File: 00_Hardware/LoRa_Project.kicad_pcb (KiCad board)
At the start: 4 copper layers, 60 x 45 mm, 87 parts, among them IC1 MAX17048G+T10, IC2 E22-900M22S, J1 Conn_01x04_Pin, J2 USB_C_Receptacle_USB2.0_16P, J3 Conn_01x04_Pin, J4 Header_01x02_2.0mm JST PH, J5 SMA_ST_SMD, J6 Conn_01x04_Pin, U1 TPS2116DRLR, U2 MIC5219-3.3YM5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

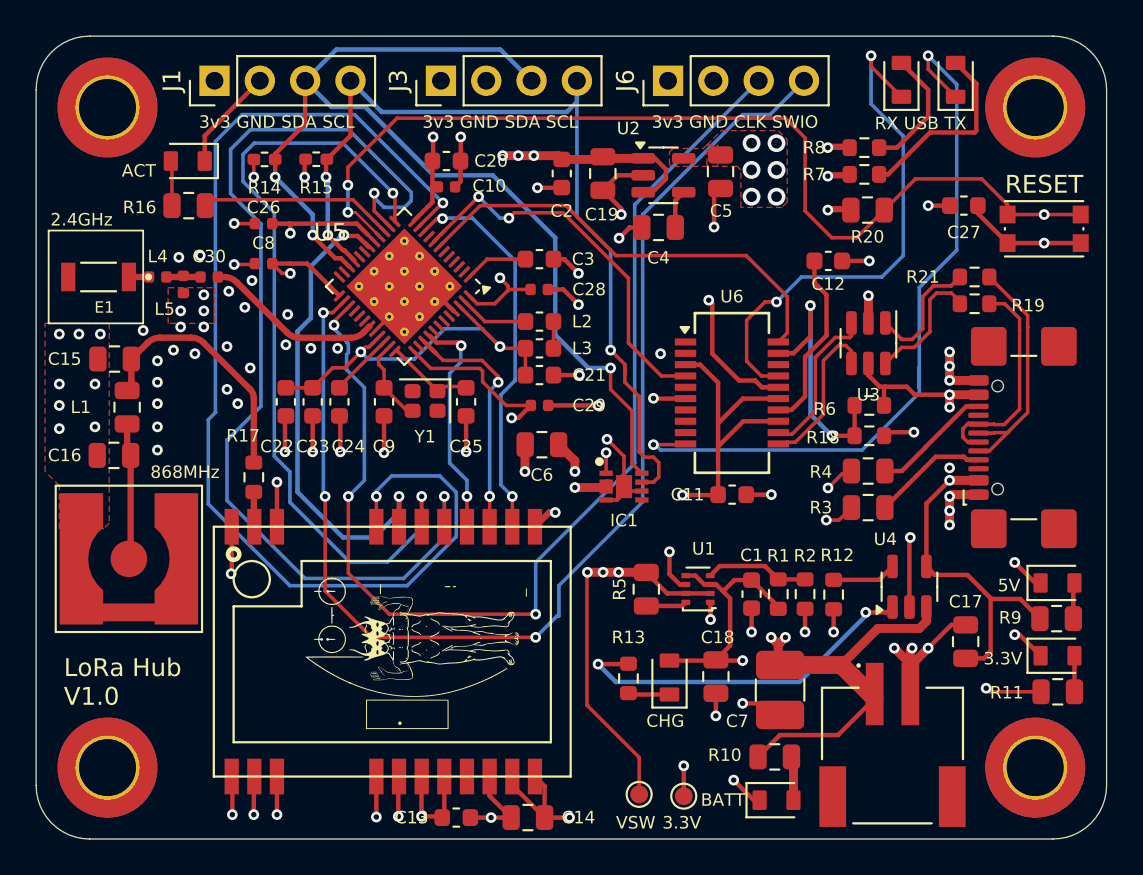
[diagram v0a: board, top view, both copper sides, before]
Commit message: Removed SMA for GPIO header placement.
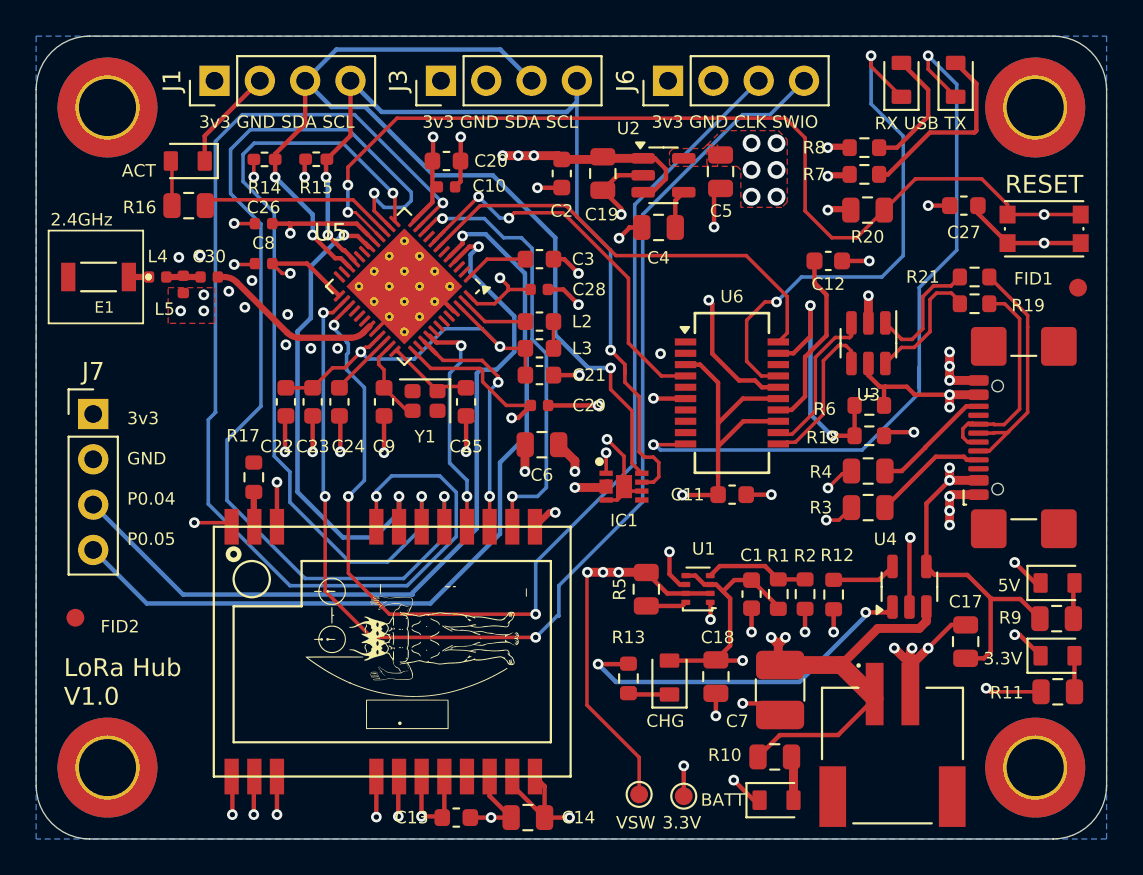
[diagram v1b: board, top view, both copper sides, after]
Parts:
- removed C15, C16: C_NP_0805, Project_Footprints:C_0805_2012Metric
- removed J5: SMA_ST_SMD, Project_Footprints:SMA_ST_SMD
- removed L1: L_jumper_0R, Project_Footprints:L_0805_2012Metric
- added FID1: Fiducial_1mm_Mask2mm, Fiducial:Fiducial_1mm_Mask2mm, F.Cu at (248.4, 66.1)
- added FID2: Fiducial_1mm_Mask2mm, Fiducial:Fiducial_1mm_Mask2mm, F.Cu at (192.2, 84.6)
- added J7: Conn_01x04_Pin, Connector_PinHeader_2.54mm:PinHeader_1x04_P2.54mm_Vertical, F.Cu at (193.2, 73.2)
- D2: value LED Green -> LED Blue
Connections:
- net Net-(R19-Pad2) renamed /Power/D_P
- net Net-(R21-Pad2) renamed /Power/D_N
- U5 pad 4: unconnected-(U5-P0.04-Pad4) -> P0.04
- U5 pad 5: unconnected-(U5-P0.05-Pad5) -> P0.05
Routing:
- net P0.05: track 0.00 -> 46.9 mm, vias 0 -> 1
- net P0.04: track 0.00 -> 45.3 mm, vias 0 -> 1
- net Net-(C15-Pad1): track 14.2 -> 0.00 mm
- net GND: track 154.7 -> 142.5 mm, vias 92 -> 70
- net Net-(J5-In): track 7.69 -> 0.00 mm
- net /nRF52840 and LoRa/LORA_IRQ: track 21.9 -> 24.6 mm
- added copper zone on B.Cu, net GND
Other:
- board text added: "3v3 GND P0.04 P0.05"
- board text removed: "868MHz"

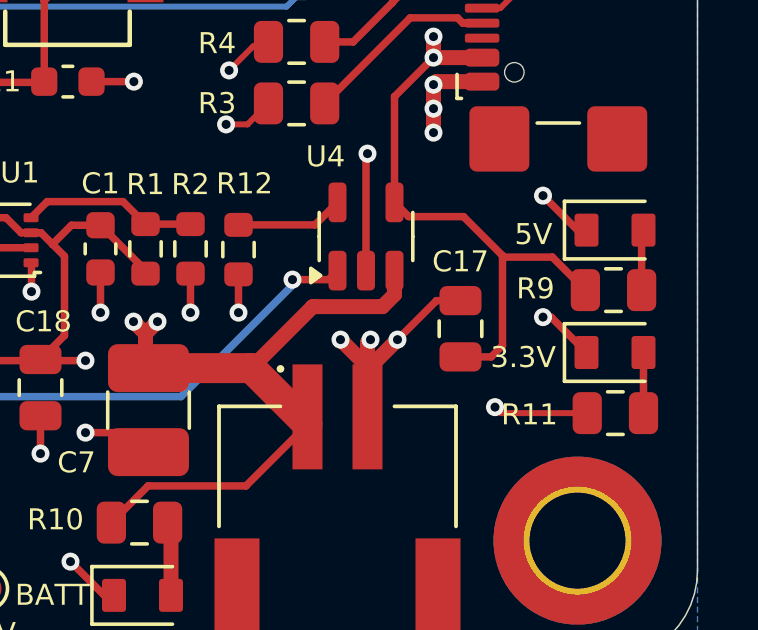
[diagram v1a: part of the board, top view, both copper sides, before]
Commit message: updated some library files/3d
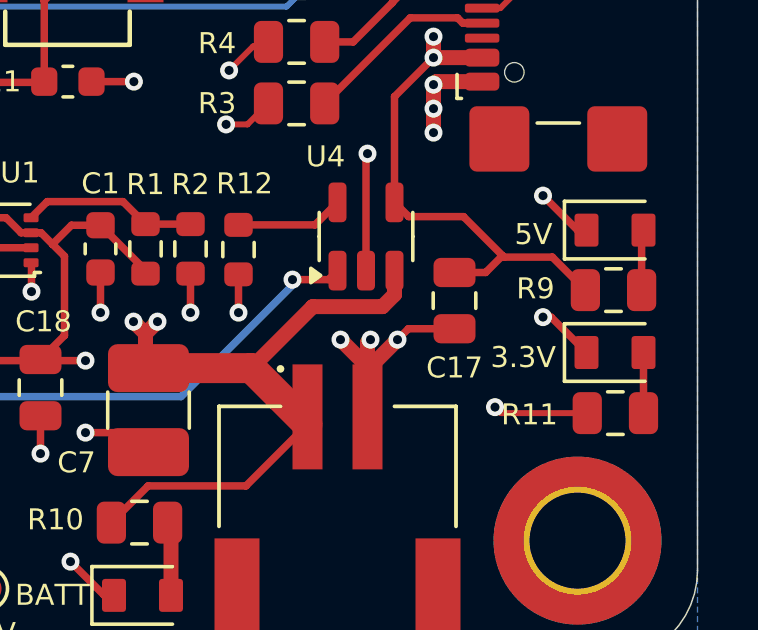
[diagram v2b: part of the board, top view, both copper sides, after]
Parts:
- moved C17 0.96 mm to (241.9, 85.0), turned to -90 degrees
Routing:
- net VBUS: track 69.0 -> 66.2 mm
- net GND: track 142.5 -> 141.9 mm

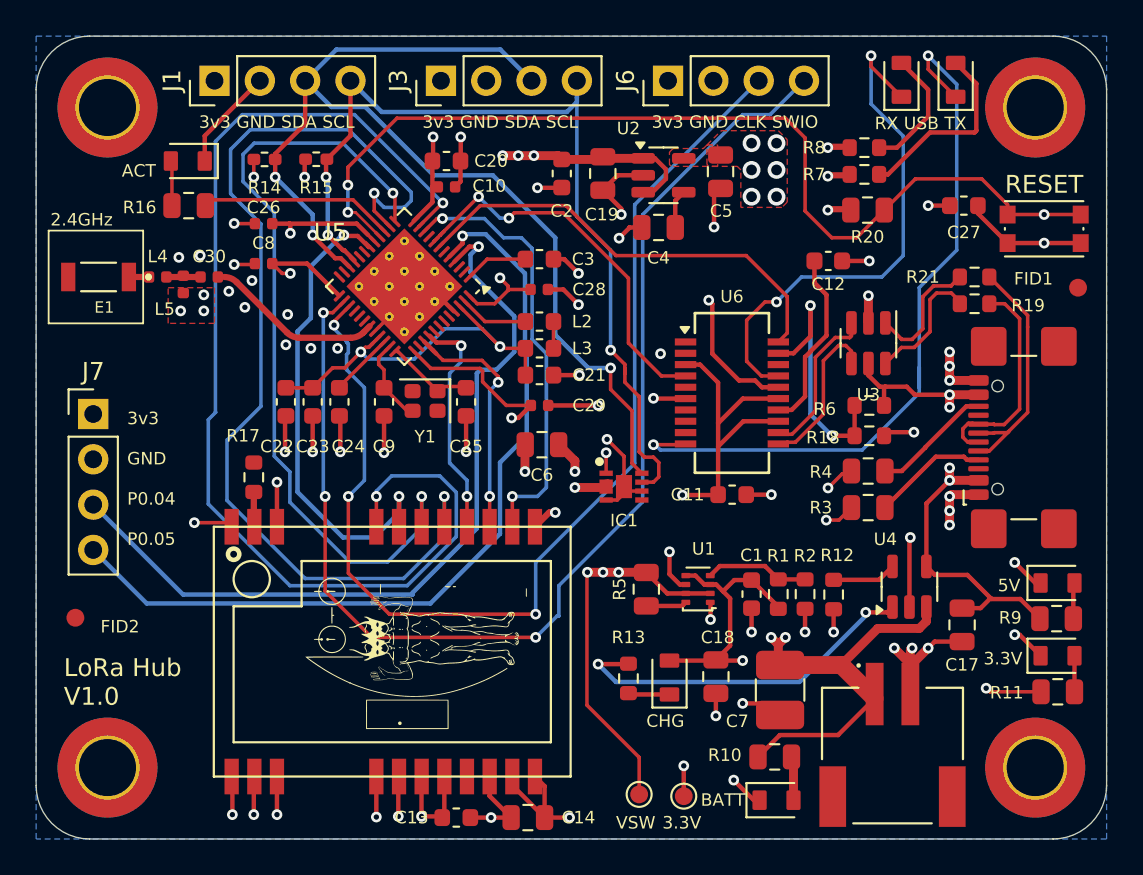
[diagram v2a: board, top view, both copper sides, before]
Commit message: Antenna output changed to fully isolate path
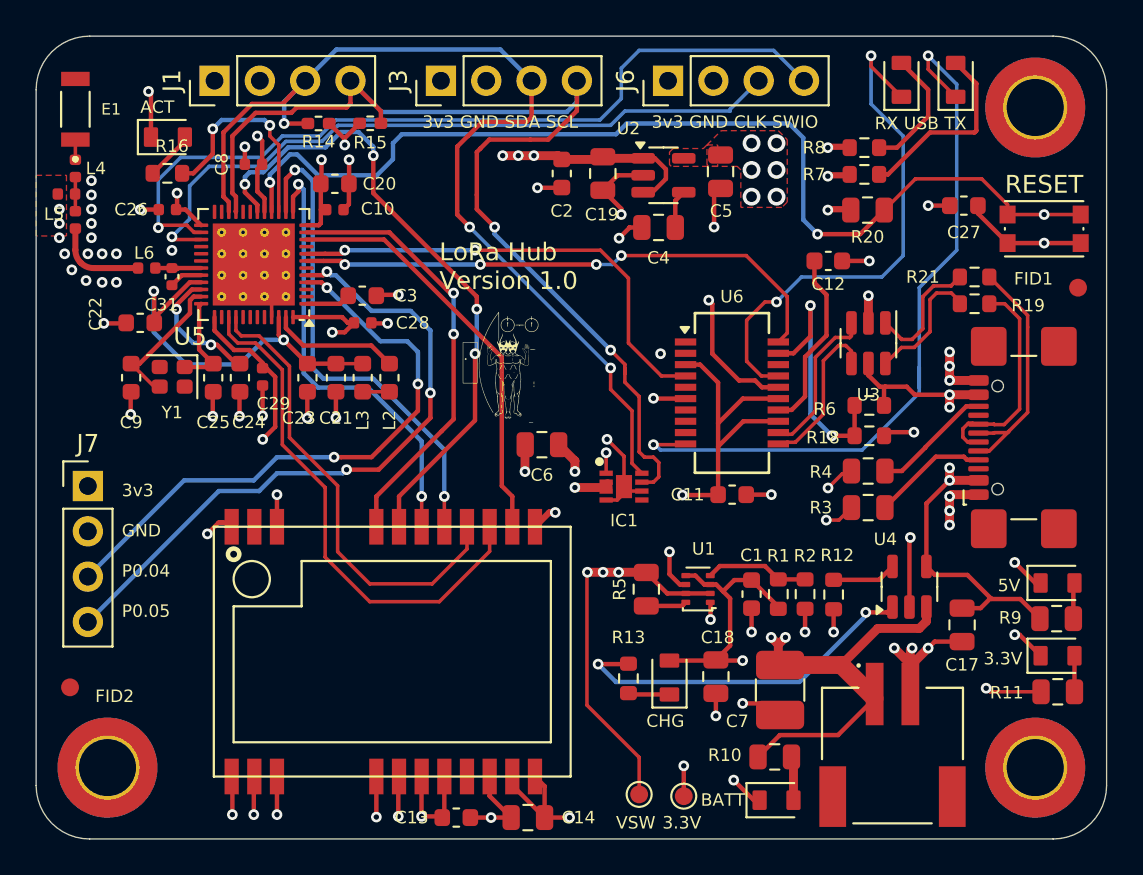
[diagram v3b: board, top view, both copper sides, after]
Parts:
- removed the G*** at (211.8, 86.1)
- removed H1: MountingHole_Pad_M3, MountingHole:MountingHole_3.2mm_M3_DIN965_Pad_TopBottom
- removed R17: 0R_0603, Resistor_SMD:R_0603_1608Metric
- added C31: 1pF, Capacitor_SMD:C_0402_1005Metric, F.Cu at (197.6, 65.5)
- added G***: LOGO, Project_Footprints:LoRa_JB, F.Cu at (216.3, 70.8)
- added L6: 4.7nH, Inductor_SMD:L_0402_1005Metric, F.Cu at (196.2, 65.0)
- R16: value 1K_0805 -> 1K_0603; footprint Project_Footprints:R_0805_2012Metric -> Resistor_SMD:R_0603_1608Metric
- moved C29 15.6 mm to (202.7, 71.1), turned to -90 degrees
- moved Y1 14.2 mm to (197.6, 71.1)
- moved C25 14.2 mm to (199.9, 71.1)
- moved C9 14.2 mm to (195.3, 71.1)
- moved C21 11.4 mm to (206.8, 71.1), turned to -90 degrees
- moved C3 10.1 mm to (208.3, 66.5)
- moved C28 10.1 mm to (208.3, 68.1)
- moved L3 10.0 mm to (208.3, 71.1), turned to -90 degrees
- moved E1 9.49 mm to (192.2, 56.1), turned to 90 degrees
- moved C22 9.29 mm to (195.8, 68.1), turned to 180 degrees
- moved L2 8.98 mm to (209.8, 71.1), turned to 90 degrees
- moved U5 8.53 mm to (202.2, 64.8), turned to 180 degrees
- moved L5 8.28 mm to (191.7, 60.9), turned to 0 degrees
- moved C30 8.15 mm to (192.2, 62.3), turned to 90 degrees
- moved L4 7.64 mm to (192.2, 59.4), turned to 90 degrees
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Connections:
- C30 pad 1: Net-(U5-ANT) -> /nRF52840 and LoRa/50Ω
- IC2 pad 21: Net-(IC2-ANT) -> unconnected-(IC2-ANT-Pad21)
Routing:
- net /nRF52840 and LoRa/LORA_SPI_CS: track 64.4 -> 26.3 mm
- net /nRF52840 and LoRa/SPI_MISO: track 57.6 -> 27.9 mm
- net SWD_CLK: track 63.0 -> 39.4 mm, vias 3 -> 1
- net SWD_IO: track 68.5 -> 46.2 mm, vias 3 -> 1
- net /nRF52840 and LoRa/SPI_MOSI: track 45.1 -> 25.4 mm
- net /nRF52840 and LoRa/LORA_BUSY: track 13.9 -> 29.1 mm, vias 2 -> 0
- net /nRF52840 and LoRa/LORA_NRST: track 12.6 -> 26.2 mm, vias 2 -> 0
- net I2C_SCL: track 51.0 -> 63.3 mm, vias 3 -> 2
- net P0.04: track 45.3 -> 33.5 mm, vias 1 -> 3
- net P0.05: track 46.9 -> 37.3 mm, vias 1 -> 3
- net /nRF52840 and LoRa/SPI_SCK: track 27.1 -> 36.3 mm, vias 2 -> 4
- net Net-(U5-ANT): track 10.2 -> 2.31 mm
- net GND: track 141.9 -> 134.7 mm, vias 70 -> 76
- net UART_RXD: track 25.3 -> 30.9 mm, vias 0 -> 4
- net /nRF52840 and LoRa/50Ω: track 0.00 -> 5.28 mm
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- removed copper zone on B.Cu, net GND
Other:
- board text added: "LoRa Hub Version 1.0"
- board text removed: "2.4GHz"
- board text removed: "LoRa Hub V1.0"

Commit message: updated silkscreen
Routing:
- net GND: track 134.7 -> 133.1 mm, vias 76 -> 82
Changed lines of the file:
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@@
 		(tags "capacitor")
 		(property "Reference" "C22"
-			(at 2.5 0.499999 90)
+			(at 2.634 -0.928 180)
 			(layer "F.SilkS")
 			(effects
@@
 		(tags "capacitor")
 		(property "Reference" "C30"
-			(at 0 1.15 90)
+			(at -1 1.5 180)
 			(layer "F.SilkS")
-			(hide yes)
 			(effects
 				(font
@@
 	)
 	(segment
-		(start 196.4365 55.2365)
-		(end 196.3 55.1)
-		(width 0.25)
-		(layer "F.Cu")
-		(net 2)
-	)
-	(segment
 		(start 235.548998 76.526)
 		(end 235.698998 76.376)
@@
 	)
 	(segment
+		(start 195.5 57.76)
+		(end 196.3345 57.76)
+		(width 0.2)
+		(layer "F.Cu")
+		(net 2)
+	)
+	(segment
 		(start 235.686499 76.3635)
 		(end 235.698999 76.376)
@@
 	)
 	(segment
+		(start 196.3345 57.76)
+		(end 196.4365 57.658)
+		(width 0.2)
+		(layer "F.Cu")
+		(net 2)
+	)
+	(segment
 		(start 242.7875 61.9375)
 		(end 242.7875 61.5)
@@
 	)
 	(segment
-		(start 196.4365 57.658)
-		(end 196.4365 55.2365)
-		(width 0.25)
-		(layer "F.Cu")
-		(net 2)
-	)
-	(segment
 		(start 230.1 85.4)
 		(end 230.1 84.062501)
@@
 	)
 	(via
+		(at 195.5 55.28)
+		(size 0.6)
+		(drill 0.3)
+		(layers "F.Cu" "B.Cu")
+		(free yes)
+		(net 2)
+	)
+	(via
 		(at 241.2 70.5)
 		(size 0.6)
@@
 	)
 	(via
+		(at 195.5 52.8)
+		(size 0.6)
+		(drill 0.3)
+		(layers "F.Cu" "B.Cu")
+		(free yes)
+		(net 2)
+	)
+	(via
 		(at 241.2 77.8)
 		(size 0.6)
@@
 	)
 	(via
+		(at 195.5 57.76)
+		(size 0.6)
+		(drill 0.3)
+		(layers "F.Cu" "B.Cu")
+		(free yes)
+		(net 2)
+	)
+	(via
+		(at 195.5 56.52)
+		(size 0.6)
+		(drill 0.3)
+		(layers "F.Cu" "B.Cu")
+		(free yes)
+		(net 2)
+	)
+	(via
 		(at 193.7 64.2)
 		(size 0.6)
@@
 	)
 	(via
+		(at 194.05 60.1)
+		(size 0.6)
+		(drill 0.3)
+		(layers "F.Cu" "B.Cu")
+		(free yes)
+		(net 2)
+	)
+	(via
 		(at 224.6 72.3)
 		(size 0.6)
@@
 	)
 	(via
+		(at 195.5 54.04)
+		(size 0.6)
+		(drill 0.3)
+		(layers "F.Cu" "B.Cu")
+		(free yes)
+		(net 2)
+	)
+	(via
 		(at 194.5 65.8)
 		(size 0.6)
@@
 	)
 	(via
-		(at 192.9 64.2)
+		(at 195.5 59)
 		(size 0.6)
 		(drill 0.3)
@@
 	)
 	(via
-		(at 196.3 55.1)
-		(size 0.6)
-		(drill 0.3)
-		(layers "F.Cu" "B.Cu")
-		(free yes)
-		(net 2)
-	)
-	(via
 		(at 219.9 95.8)
 		(size 0.6)
@@
 		(size 0.6)
 		(drill 0.3)
+		(layers "F.Cu" "B.Cu")
+		(free yes)
+		(net 2)
+	)
+	(via
+		(at 195 60.1)
+		(size 0.6)
+		(drill 0.3)

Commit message: updated from generated script
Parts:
- removed G***: LOGO, Project_Footprints:LoRa_JB
- R1, R2: value 100K -> 100k
- R10, R9: value 1K5_0805 -> 1.5k
- R11: value 1K_0805 -> 1k
- R12: value 10K0_0603 -> 10k
- R16: value 1K_0603 -> 1k
- R18, R20, R5: value 10K -> 10k
- R19, R21: value 27 -> 27R
- R3, R4: value 5K1_0805 -> 5.1k
- R7, R8: value 270R_0603 -> 270R
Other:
- board text added: "github.com/JBeeBK"

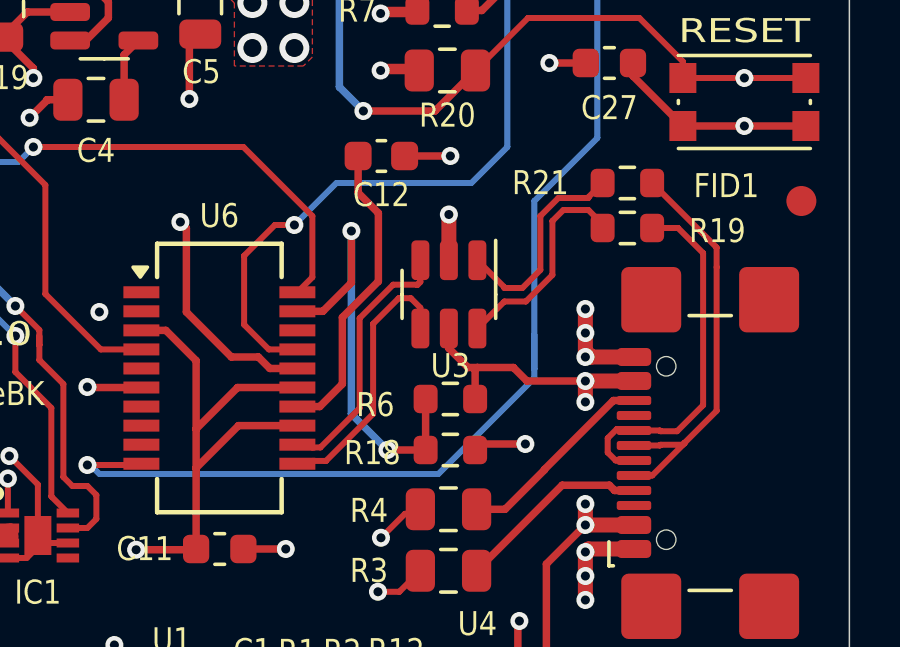
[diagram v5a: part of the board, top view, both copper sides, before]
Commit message: Added V1.0 assembly and testing notes, removed traces from ESD to move it V1.1
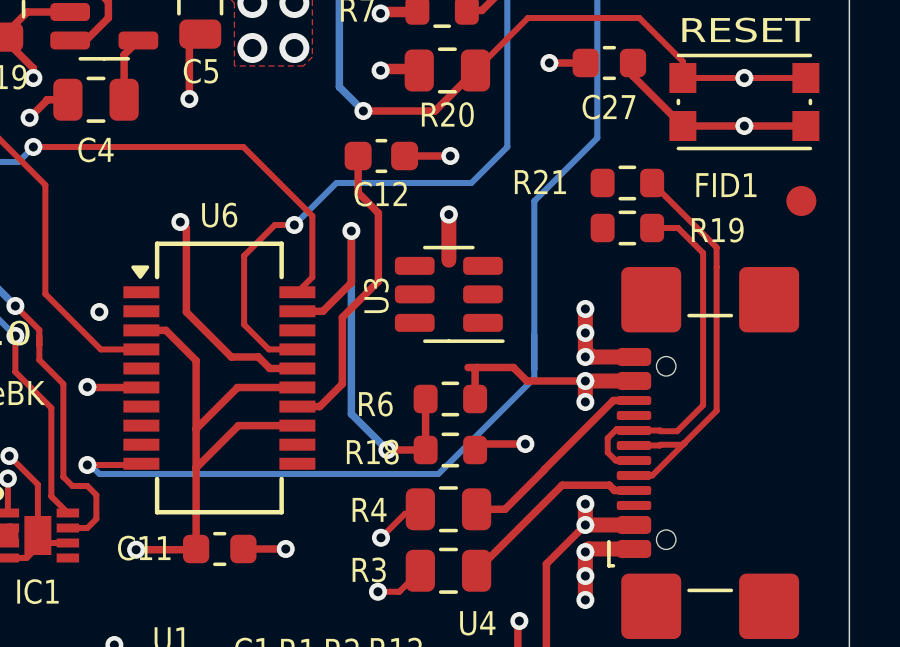
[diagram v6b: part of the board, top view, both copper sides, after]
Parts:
- turned U3 to 180 degrees
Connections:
- U3 pad 3: D- -> /Power/D_P
- U3 pad 6: /Power/D_P -> D-
- Y1 pad : Net-(U5-XC1) -> (no net)
- Y1 pad 2: (no net) -> Net-(U5-XC1)
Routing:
- net D+: track 8.97 -> 0.00 mm
- net D-: track 8.91 -> 0.00 mm
- net /Power/D_P: track 7.19 -> 0.00 mm
- net /Power/D_N: track 7.09 -> 0.00 mm
- net VBUS: track 66.2 -> 64.7 mm
